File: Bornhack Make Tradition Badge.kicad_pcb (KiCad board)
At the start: 2 copper layers, 100 x 100 mm, 45 parts, among them J1 DEBUG, J2 LE UART, J3 I2C, J4 CONN_02X04, J5 CONN_02X04, J6 CONN_02X04, J7 CONN_01X02, J8 CONN_01X02, P1 USB_OTG, Q1 FDC6420C, SW1 RESET, SW2 POWER, SW3 UP, SW4 DOWN, SW5 RIGHT, SW6 LEFT, U1 EFM32HG322

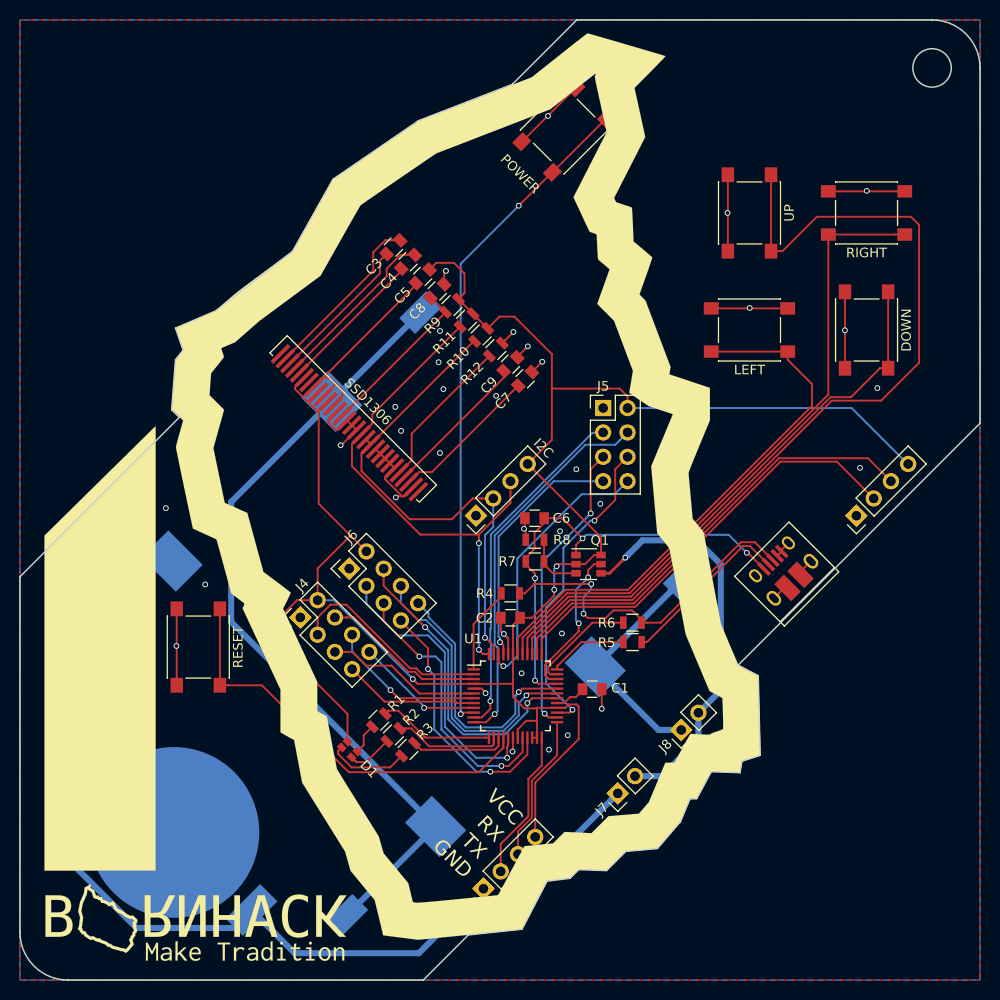
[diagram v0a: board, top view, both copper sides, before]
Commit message: Flipped D+ and D- and removed dual battery option
- D+ and D- has been corrected
- Coin cell holder has been removed, since the badge uses too much power when the screen is on for a coin cell to be a reasonable power source.
- Current measurement pin headers have also been removed.

Signed-off-by: Thomas Flummer <tf@flummer.net>
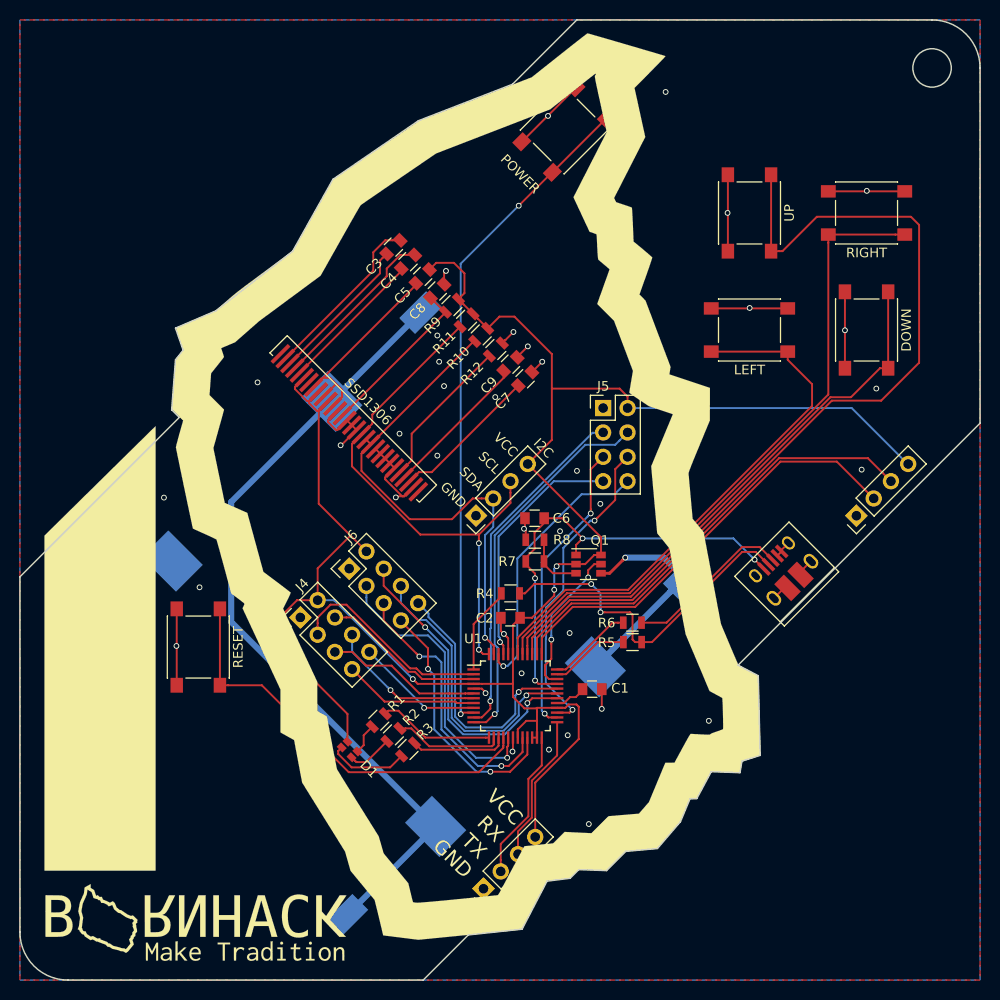
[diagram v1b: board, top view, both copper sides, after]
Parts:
- removed BT1: 3V Button cell, Power:Linx_BAT_HLD_001
- removed J7, J8: CONN_01X02, Pin_Headers:Pin_Header_Straight_1x02_Pitch2.54mm
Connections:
- BT2 pad 1: Net-(BT2-Pad1) -> VBAT
- R4 pad 1: Net-(P1-Pad3) -> Net-(P1-Pad2)
- U1 pad 35: Net-(R6-Pad2) -> Net-(R5-Pad2)
- U1 pad 36: Net-(R5-Pad2) -> Net-(R6-Pad2)
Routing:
- net Net-(BT1-Pad1): track 81.0 -> 0.00 mm
- net Net-(BT2-Pad1): track 24.7 -> 0.00 mm
- net VBAT: track 42.3 -> 23.3 mm
- net Net-(P1-Pad3): track 36.5 -> 17.8 mm, vias 2 -> 0
- net Net-(P1-Pad2): track 18.1 -> 35.9 mm, vias 0 -> 2
- net Net-(R6-Pad2): track 11.3 -> 8.91 mm
- net GND: vias 37 -> 34
- net (no net): vias 0 -> 5
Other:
- board text added: "SCL"
- board text added: "SDA"
- board text removed: "DEVELOPER"
- board text removed: "EDITION"

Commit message: Changed pins for 2 buttons, cleanup and proto pads
- Changed the pins for the LEFT (X) and RIGHT (Y) buttons so that all buttons have their own interrupt
- Changed the name of the buttons to A, B, X and Y so that the names also make sense, when the badge is oriented differently
- Removed silkscreen lines around buttons and non populated pin headers
- Added SMD prototyping area on the back
- Added Open Hardware Logo and CC-BY-SA graphics
- Updated gerber files (production run)

Signed-off-by: Thomas Flummer <tf@flummer.net>
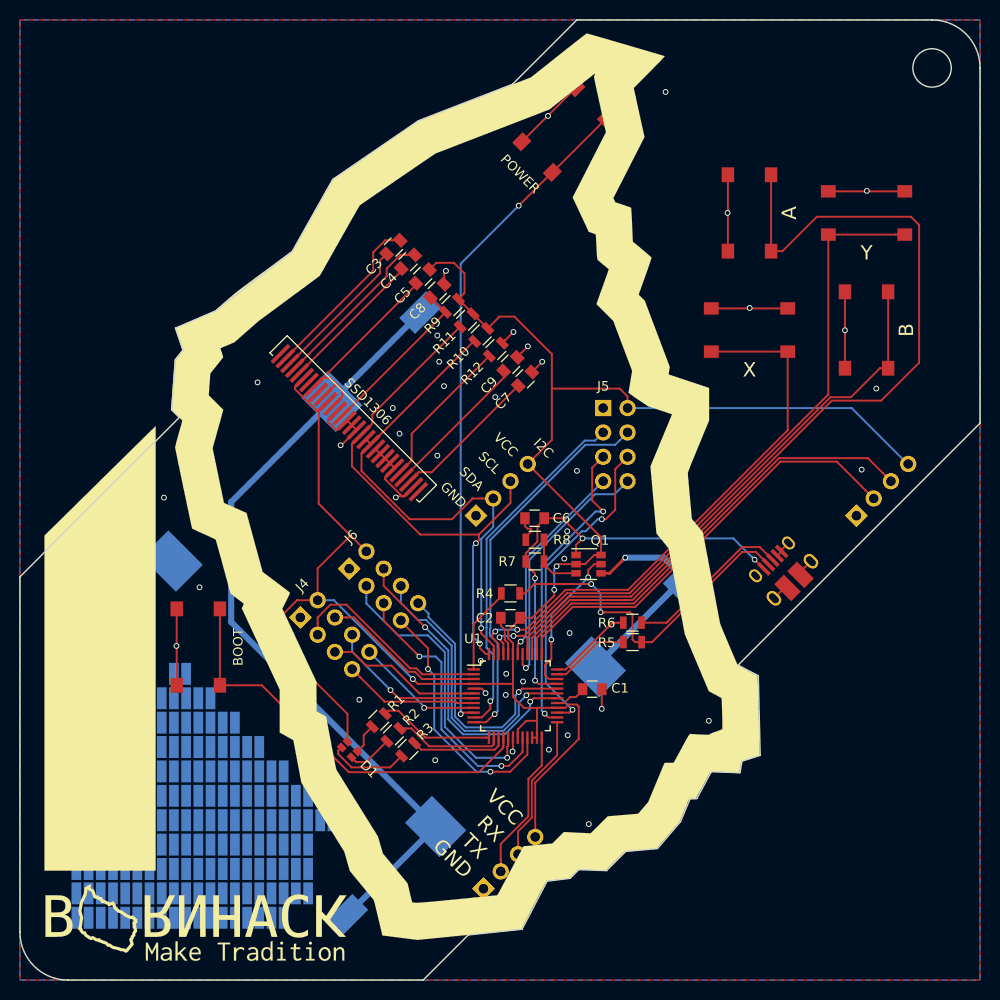
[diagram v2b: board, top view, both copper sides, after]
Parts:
- added G***: LOGO, Aesthetics:oshw_logo_8.3mm, B.Cu at (116.2, 83.3)
- added G***: LOGO, labitat_kicad_footprints:cc-by-sa_badge_8mm, B.Cu at (123.8, 76.2)
- added REF**: SMD Proto pad, ConnectorsTF:SMD_Proto_pad, B.Cu at (82.5, 133.3)
- added REF**: SMD Proto pad, ConnectorsTF:SMD_Proto_pad, B.Cu at (77.5, 128.3)
- added REF**: SMD Proto pad, ConnectorsTF:SMD_Proto_pad, B.Cu at (62.2, 133.3)
- added REF**: SMD Proto pad, ConnectorsTF:SMD_Proto_pad, B.Cu at (61.0, 133.3)
- added REF**: SMD Proto pad, ConnectorsTF:SMD_Proto_pad, B.Cu at (59.7, 133.3)
- added REF**: SMD Proto pad, ConnectorsTF:SMD_Proto_pad, B.Cu at (58.4, 133.3)
- added REF**: SMD Proto pad, ConnectorsTF:SMD_Proto_pad, B.Cu at (57.1, 133.3)
- added REF**: SMD Proto pad, ConnectorsTF:SMD_Proto_pad, B.Cu at (55.9, 133.3)
- added REF**: SMD Proto pad, ConnectorsTF:SMD_Proto_pad, B.Cu at (55.9, 135.9)
- added REF**: SMD Proto pad, ConnectorsTF:SMD_Proto_pad, B.Cu at (57.1, 135.9)
- added REF**: SMD Proto pad, ConnectorsTF:SMD_Proto_pad, B.Cu at (58.4, 135.9)
- added REF**: SMD Proto pad, ConnectorsTF:SMD_Proto_pad, B.Cu at (59.7, 135.9)
- added REF**: SMD Proto pad, ConnectorsTF:SMD_Proto_pad, B.Cu at (74.9, 125.7)
- added REF**: SMD Proto pad, ConnectorsTF:SMD_Proto_pad, B.Cu at (61.0, 135.9)
- added REF**: SMD Proto pad, ConnectorsTF:SMD_Proto_pad, B.Cu at (62.2, 135.9)
- added REF**: SMD Proto pad, ConnectorsTF:SMD_Proto_pad, B.Cu at (63.5, 135.9)
- added REF**: SMD Proto pad, ConnectorsTF:SMD_Proto_pad, B.Cu at (64.8, 135.9)
- added REF**: SMD Proto pad, ConnectorsTF:SMD_Proto_pad, B.Cu at (66.0, 135.9)
- added REF**: SMD Proto pad, ConnectorsTF:SMD_Proto_pad, B.Cu at (67.3, 135.9)
- added REF**: SMD Proto pad, ConnectorsTF:SMD_Proto_pad, B.Cu at (68.6, 135.9)
- added REF**: SMD Proto pad, ConnectorsTF:SMD_Proto_pad, B.Cu at (69.8, 135.9)
- added REF**: SMD Proto pad, ConnectorsTF:SMD_Proto_pad, B.Cu at (71.1, 135.9)
- added REF**: SMD Proto pad, ConnectorsTF:SMD_Proto_pad, B.Cu at (72.4, 135.9)
- added REF**: SMD Proto pad, ConnectorsTF:SMD_Proto_pad, B.Cu at (72.4, 123.2)
- added REF**: SMD Proto pad, ConnectorsTF:SMD_Proto_pad, B.Cu at (73.7, 135.9)
- added REF**: SMD Proto pad, ConnectorsTF:SMD_Proto_pad, B.Cu at (74.9, 135.9)
- added REF**: SMD Proto pad, ConnectorsTF:SMD_Proto_pad, B.Cu at (76.2, 135.9)
- added REF**: SMD Proto pad, ConnectorsTF:SMD_Proto_pad, B.Cu at (77.5, 135.9)
- added REF**: SMD Proto pad, ConnectorsTF:SMD_Proto_pad, B.Cu at (78.7, 135.9)
- added REF**: SMD Proto pad, ConnectorsTF:SMD_Proto_pad, B.Cu at (78.7, 138.4)
- added REF**: SMD Proto pad, ConnectorsTF:SMD_Proto_pad, B.Cu at (77.5, 138.4)
- added REF**: SMD Proto pad, ConnectorsTF:SMD_Proto_pad, B.Cu at (76.2, 138.4)
- added REF**: SMD Proto pad, ConnectorsTF:SMD_Proto_pad, B.Cu at (74.9, 138.4)
- added REF**: SMD Proto pad, ConnectorsTF:SMD_Proto_pad, B.Cu at (73.7, 138.4)
- added REF**: SMD Proto pad, ConnectorsTF:SMD_Proto_pad, B.Cu at (69.8, 120.7)
- added REF**: SMD Proto pad, ConnectorsTF:SMD_Proto_pad, B.Cu at (71.1, 138.4)
- added REF**: SMD Proto pad, ConnectorsTF:SMD_Proto_pad, B.Cu at (72.4, 138.4)
- added REF**: SMD Proto pad, ConnectorsTF:SMD_Proto_pad, B.Cu at (69.8, 138.4)
- added REF**: SMD Proto pad, ConnectorsTF:SMD_Proto_pad, B.Cu at (68.6, 138.4)
- added REF**: SMD Proto pad, ConnectorsTF:SMD_Proto_pad, B.Cu at (67.3, 138.4)
- added REF**: SMD Proto pad, ConnectorsTF:SMD_Proto_pad, B.Cu at (66.0, 138.4)
- added REF**: SMD Proto pad, ConnectorsTF:SMD_Proto_pad, B.Cu at (64.8, 138.4)
- added REF**: SMD Proto pad, ConnectorsTF:SMD_Proto_pad, B.Cu at (63.5, 138.4)
- added REF**: SMD Proto pad, ConnectorsTF:SMD_Proto_pad, B.Cu at (62.2, 138.4)
- added REF**: SMD Proto pad, ConnectorsTF:SMD_Proto_pad, B.Cu at (61.0, 138.4)
- added REF**: SMD Proto pad, ConnectorsTF:SMD_Proto_pad, B.Cu at (68.6, 120.7)
- added REF**: SMD Proto pad, ConnectorsTF:SMD_Proto_pad, B.Cu at (59.7, 138.4)
- added REF**: SMD Proto pad, ConnectorsTF:SMD_Proto_pad, B.Cu at (58.4, 138.4)
- added REF**: SMD Proto pad, ConnectorsTF:SMD_Proto_pad, B.Cu at (57.1, 138.4)
- added REF**: SMD Proto pad, ConnectorsTF:SMD_Proto_pad, B.Cu at (55.9, 138.4)
- added REF**: SMD Proto pad, ConnectorsTF:SMD_Proto_pad, B.Cu at (63.5, 141.0)
- added REF**: SMD Proto pad, ConnectorsTF:SMD_Proto_pad, B.Cu at (64.8, 141.0)
- added REF**: SMD Proto pad, ConnectorsTF:SMD_Proto_pad, B.Cu at (66.0, 141.0)
- added REF**: SMD Proto pad, ConnectorsTF:SMD_Proto_pad, B.Cu at (67.3, 141.0)
- added REF**: SMD Proto pad, ConnectorsTF:SMD_Proto_pad, B.Cu at (68.6, 141.0)
- added REF**: SMD Proto pad, ConnectorsTF:SMD_Proto_pad, B.Cu at (69.8, 141.0)
- added REF**: SMD Proto pad, ConnectorsTF:SMD_Proto_pad, B.Cu at (67.3, 120.7)
- added REF**: SMD Proto pad, ConnectorsTF:SMD_Proto_pad, B.Cu at (71.1, 141.0)
- added REF**: SMD Proto pad, ConnectorsTF:SMD_Proto_pad, B.Cu at (72.4, 141.0)
- added REF**: SMD Proto pad, ConnectorsTF:SMD_Proto_pad, B.Cu at (73.7, 141.0)
- added REF**: SMD Proto pad, ConnectorsTF:SMD_Proto_pad, B.Cu at (74.9, 141.0)
- added REF**: SMD Proto pad, ConnectorsTF:SMD_Proto_pad, B.Cu at (76.2, 141.0)
- added REF**: SMD Proto pad, ConnectorsTF:SMD_Proto_pad, B.Cu at (77.5, 141.0)
- added REF**: SMD Proto pad, ConnectorsTF:SMD_Proto_pad, B.Cu at (78.7, 141.0)
- added REF**: SMD Proto pad, ConnectorsTF:SMD_Proto_pad, B.Cu at (77.5, 143.5)
- added REF**: SMD Proto pad, ConnectorsTF:SMD_Proto_pad, B.Cu at (76.2, 143.5)
- added REF**: SMD Proto pad, ConnectorsTF:SMD_Proto_pad, B.Cu at (74.9, 143.5)
- added REF**: SMD Proto pad, ConnectorsTF:SMD_Proto_pad, B.Cu at (66.0, 120.7)
- added REF**: SMD Proto pad, ConnectorsTF:SMD_Proto_pad, B.Cu at (73.7, 143.5)
- added REF**: SMD Proto pad, ConnectorsTF:SMD_Proto_pad, B.Cu at (72.4, 143.5)
- added REF**: SMD Proto pad, ConnectorsTF:SMD_Proto_pad, B.Cu at (71.1, 143.5)
- added REF**: SMD Proto pad, ConnectorsTF:SMD_Proto_pad, B.Cu at (69.8, 143.5)
- added REF**: SMD Proto pad, ConnectorsTF:SMD_Proto_pad, B.Cu at (68.6, 143.5)
- added REF**: SMD Proto pad, ConnectorsTF:SMD_Proto_pad, B.Cu at (67.3, 143.5)
- added REF**: SMD Proto pad, ConnectorsTF:SMD_Proto_pad, B.Cu at (66.0, 143.5)
- added REF**: SMD Proto pad, ConnectorsTF:SMD_Proto_pad, B.Cu at (64.8, 143.5)
- added REF**: SMD Proto pad, ConnectorsTF:SMD_Proto_pad, B.Cu at (63.5, 143.5)
- added REF**: SMD Proto pad, ConnectorsTF:SMD_Proto_pad, B.Cu at (55.9, 141.0)
- added REF**: SMD Proto pad, ConnectorsTF:SMD_Proto_pad, B.Cu at (64.8, 120.7)
- added REF**: SMD Proto pad, ConnectorsTF:SMD_Proto_pad, B.Cu at (57.1, 141.0)
- added REF**: SMD Proto pad, ConnectorsTF:SMD_Proto_pad, B.Cu at (58.4, 141.0)
- added REF**: SMD Proto pad, ConnectorsTF:SMD_Proto_pad, B.Cu at (59.7, 141.0)
- added REF**: SMD Proto pad, ConnectorsTF:SMD_Proto_pad, B.Cu at (61.0, 141.0)
- added REF**: SMD Proto pad, ConnectorsTF:SMD_Proto_pad, B.Cu at (62.2, 141.0)
- added REF**: SMD Proto pad, ConnectorsTF:SMD_Proto_pad, B.Cu at (62.2, 143.5)
- added REF**: SMD Proto pad, ConnectorsTF:SMD_Proto_pad, B.Cu at (61.0, 143.5)
- added REF**: SMD Proto pad, ConnectorsTF:SMD_Proto_pad, B.Cu at (59.7, 143.5)
- added REF**: SMD Proto pad, ConnectorsTF:SMD_Proto_pad, B.Cu at (58.4, 143.5)
- added REF**: SMD Proto pad, ConnectorsTF:SMD_Proto_pad, B.Cu at (57.1, 143.5)
- added REF**: SMD Proto pad, ConnectorsTF:SMD_Proto_pad, B.Cu at (63.5, 120.7)
- added REF**: SMD Proto pad, ConnectorsTF:SMD_Proto_pad, B.Cu at (55.9, 143.5)
- added REF**: SMD Proto pad, ConnectorsTF:SMD_Proto_pad, B.Cu at (62.2, 120.7)
- added REF**: SMD Proto pad, ConnectorsTF:SMD_Proto_pad, B.Cu at (81.3, 133.3)
- added REF**: SMD Proto pad, ConnectorsTF:SMD_Proto_pad, B.Cu at (61.0, 120.7)
- added REF**: SMD Proto pad, ConnectorsTF:SMD_Proto_pad, B.Cu at (59.7, 120.7)
- added REF**: SMD Proto pad, ConnectorsTF:SMD_Proto_pad, B.Cu at (58.4, 120.7)
- added REF**: SMD Proto pad, ConnectorsTF:SMD_Proto_pad, B.Cu at (71.1, 123.2)
- added REF**: SMD Proto pad, ConnectorsTF:SMD_Proto_pad, B.Cu at (69.8, 123.2)
- added REF**: SMD Proto pad, ConnectorsTF:SMD_Proto_pad, B.Cu at (68.6, 123.2)
- added REF**: SMD Proto pad, ConnectorsTF:SMD_Proto_pad, B.Cu at (67.3, 123.2)
- added REF**: SMD Proto pad, ConnectorsTF:SMD_Proto_pad, B.Cu at (66.0, 123.2)
- added REF**: SMD Proto pad, ConnectorsTF:SMD_Proto_pad, B.Cu at (64.8, 123.2)
- added REF**: SMD Proto pad, ConnectorsTF:SMD_Proto_pad, B.Cu at (63.5, 123.2)
- added REF**: SMD Proto pad, ConnectorsTF:SMD_Proto_pad, B.Cu at (66.0, 118.1)
- added REF**: SMD Proto pad, ConnectorsTF:SMD_Proto_pad, B.Cu at (62.2, 123.2)
- added REF**: SMD Proto pad, ConnectorsTF:SMD_Proto_pad, B.Cu at (61.0, 123.2)
- added REF**: SMD Proto pad, ConnectorsTF:SMD_Proto_pad, B.Cu at (59.7, 123.2)
- added REF**: SMD Proto pad, ConnectorsTF:SMD_Proto_pad, B.Cu at (58.4, 123.2)
- added REF**: SMD Proto pad, ConnectorsTF:SMD_Proto_pad, B.Cu at (57.1, 123.2)
- added REF**: SMD Proto pad, ConnectorsTF:SMD_Proto_pad, B.Cu at (55.9, 123.2)
- added REF**: SMD Proto pad, ConnectorsTF:SMD_Proto_pad, B.Cu at (55.9, 125.7)
- added REF**: SMD Proto pad, ConnectorsTF:SMD_Proto_pad, B.Cu at (57.1, 125.7)
- added REF**: SMD Proto pad, ConnectorsTF:SMD_Proto_pad, B.Cu at (58.4, 125.7)
- added REF**: SMD Proto pad, ConnectorsTF:SMD_Proto_pad, B.Cu at (59.7, 125.7)
- added REF**: SMD Proto pad, ConnectorsTF:SMD_Proto_pad, B.Cu at (67.3, 118.1)
- added REF**: SMD Proto pad, ConnectorsTF:SMD_Proto_pad, B.Cu at (61.0, 125.7)
- added REF**: SMD Proto pad, ConnectorsTF:SMD_Proto_pad, B.Cu at (62.2, 125.7)
- added REF**: SMD Proto pad, ConnectorsTF:SMD_Proto_pad, B.Cu at (63.5, 125.7)
- added REF**: SMD Proto pad, ConnectorsTF:SMD_Proto_pad, B.Cu at (64.8, 125.7)
- added REF**: SMD Proto pad, ConnectorsTF:SMD_Proto_pad, B.Cu at (66.0, 125.7)
- added REF**: SMD Proto pad, ConnectorsTF:SMD_Proto_pad, B.Cu at (68.6, 125.7)
- added REF**: SMD Proto pad, ConnectorsTF:SMD_Proto_pad, B.Cu at (67.3, 125.7)
- added REF**: SMD Proto pad, ConnectorsTF:SMD_Proto_pad, B.Cu at (69.8, 125.7)
- added REF**: SMD Proto pad, ConnectorsTF:SMD_Proto_pad, B.Cu at (71.1, 125.7)
- added REF**: SMD Proto pad, ConnectorsTF:SMD_Proto_pad, B.Cu at (72.4, 125.7)
- added REF**: SMD Proto pad, ConnectorsTF:SMD_Proto_pad, B.Cu at (80.0, 141.0)
- added REF**: SMD Proto pad, ConnectorsTF:SMD_Proto_pad, B.Cu at (73.7, 125.7)
- added REF**: SMD Proto pad, ConnectorsTF:SMD_Proto_pad, B.Cu at (76.2, 128.3)
- added REF**: SMD Proto pad, ConnectorsTF:SMD_Proto_pad, B.Cu at (74.9, 128.3)
- added REF**: SMD Proto pad, ConnectorsTF:SMD_Proto_pad, B.Cu at (73.7, 128.3)
- added REF**: SMD Proto pad, ConnectorsTF:SMD_Proto_pad, B.Cu at (72.4, 128.3)
- added REF**: SMD Proto pad, ConnectorsTF:SMD_Proto_pad, B.Cu at (71.1, 128.3)
- added REF**: SMD Proto pad, ConnectorsTF:SMD_Proto_pad, B.Cu at (69.8, 128.3)
- added REF**: SMD Proto pad, ConnectorsTF:SMD_Proto_pad, B.Cu at (68.6, 128.3)
- added REF**: SMD Proto pad, ConnectorsTF:SMD_Proto_pad, B.Cu at (67.3, 128.3)
- added REF**: SMD Proto pad, ConnectorsTF:SMD_Proto_pad, B.Cu at (66.0, 128.3)
- added REF**: SMD Proto pad, ConnectorsTF:SMD_Proto_pad, B.Cu at (80.0, 138.4)
- added REF**: SMD Proto pad, ConnectorsTF:SMD_Proto_pad, B.Cu at (64.8, 128.3)
- added REF**: SMD Proto pad, ConnectorsTF:SMD_Proto_pad, B.Cu at (63.5, 128.3)
- added REF**: SMD Proto pad, ConnectorsTF:SMD_Proto_pad, B.Cu at (62.2, 128.3)
- added REF**: SMD Proto pad, ConnectorsTF:SMD_Proto_pad, B.Cu at (61.0, 128.3)
- added REF**: SMD Proto pad, ConnectorsTF:SMD_Proto_pad, B.Cu at (59.7, 128.3)
- added REF**: SMD Proto pad, ConnectorsTF:SMD_Proto_pad, B.Cu at (58.4, 128.3)
- added REF**: SMD Proto pad, ConnectorsTF:SMD_Proto_pad, B.Cu at (57.1, 128.3)
- added REF**: SMD Proto pad, ConnectorsTF:SMD_Proto_pad, B.Cu at (55.9, 128.3)
- added REF**: SMD Proto pad, ConnectorsTF:SMD_Proto_pad, B.Cu at (55.9, 130.8)
- added REF**: SMD Proto pad, ConnectorsTF:SMD_Proto_pad, B.Cu at (57.1, 130.8)
- added REF**: SMD Proto pad, ConnectorsTF:SMD_Proto_pad, B.Cu at (80.0, 135.9)
- added REF**: SMD Proto pad, ConnectorsTF:SMD_Proto_pad, B.Cu at (59.7, 130.8)
- added REF**: SMD Proto pad, ConnectorsTF:SMD_Proto_pad, B.Cu at (58.4, 130.8)
- added REF**: SMD Proto pad, ConnectorsTF:SMD_Proto_pad, B.Cu at (61.0, 130.8)
- added REF**: SMD Proto pad, ConnectorsTF:SMD_Proto_pad, B.Cu at (62.2, 130.8)
- added REF**: SMD Proto pad, ConnectorsTF:SMD_Proto_pad, B.Cu at (63.5, 130.8)
- added REF**: SMD Proto pad, ConnectorsTF:SMD_Proto_pad, B.Cu at (64.8, 130.8)
- added REF**: SMD Proto pad, ConnectorsTF:SMD_Proto_pad, B.Cu at (66.0, 130.8)
- added REF**: SMD Proto pad, ConnectorsTF:SMD_Proto_pad, B.Cu at (67.3, 130.8)
- added REF**: SMD Proto pad, ConnectorsTF:SMD_Proto_pad, B.Cu at (68.6, 130.8)
- added REF**: SMD Proto pad, ConnectorsTF:SMD_Proto_pad, B.Cu at (69.8, 130.8)
- added REF**: SMD Proto pad, ConnectorsTF:SMD_Proto_pad, B.Cu at (80.0, 133.3)
- added REF**: SMD Proto pad, ConnectorsTF:SMD_Proto_pad, B.Cu at (71.1, 130.8)
- added REF**: SMD Proto pad, ConnectorsTF:SMD_Proto_pad, B.Cu at (72.4, 130.8)
- added REF**: SMD Proto pad, ConnectorsTF:SMD_Proto_pad, B.Cu at (73.7, 130.8)
- added REF**: SMD Proto pad, ConnectorsTF:SMD_Proto_pad, B.Cu at (74.9, 130.8)
- added REF**: SMD Proto pad, ConnectorsTF:SMD_Proto_pad, B.Cu at (76.2, 130.8)
- added REF**: SMD Proto pad, ConnectorsTF:SMD_Proto_pad, B.Cu at (77.5, 130.8)
- added REF**: SMD Proto pad, ConnectorsTF:SMD_Proto_pad, B.Cu at (78.7, 130.8)
- added REF**: SMD Proto pad, ConnectorsTF:SMD_Proto_pad, B.Cu at (78.7, 133.3)
- added REF**: SMD Proto pad, ConnectorsTF:SMD_Proto_pad, B.Cu at (77.5, 133.3)
- added REF**: SMD Proto pad, ConnectorsTF:SMD_Proto_pad, B.Cu at (76.2, 133.3)
- added REF**: SMD Proto pad, ConnectorsTF:SMD_Proto_pad, B.Cu at (80.0, 130.8)
- added REF**: SMD Proto pad, ConnectorsTF:SMD_Proto_pad, B.Cu at (74.9, 133.3)
- added REF**: SMD Proto pad, ConnectorsTF:SMD_Proto_pad, B.Cu at (73.7, 133.3)
- added REF**: SMD Proto pad, ConnectorsTF:SMD_Proto_pad, B.Cu at (72.4, 133.3)
- added REF**: SMD Proto pad, ConnectorsTF:SMD_Proto_pad, B.Cu at (71.1, 133.3)
- added REF**: SMD Proto pad, ConnectorsTF:SMD_Proto_pad, B.Cu at (69.8, 133.3)
- added REF**: SMD Proto pad, ConnectorsTF:SMD_Proto_pad, B.Cu at (68.6, 133.3)
- added REF**: SMD Proto pad, ConnectorsTF:SMD_Proto_pad, B.Cu at (67.3, 133.3)
- added REF**: SMD Proto pad, ConnectorsTF:SMD_Proto_pad, B.Cu at (66.0, 133.3)
- added REF**: SMD Proto pad, ConnectorsTF:SMD_Proto_pad, B.Cu at (64.8, 133.3)
- added REF**: SMD Proto pad, ConnectorsTF:SMD_Proto_pad, B.Cu at (63.5, 133.3)
- R2: value 1K -> 1.2K
- R3: value 1K -> 820
- SW1: value RESET -> BOOT
- SW3: value UP -> A
- SW4: value DOWN -> B
- SW5: value RIGHT -> Y
- SW6: value LEFT -> X
- moved G*** 0.08 mm to (101.9, 99.0)
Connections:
- net DOWN renamed BUTTON_B
- net UP renamed BUTTON_A
- J5 pad 7: PE10 -> PF5
- J5 pad 8: PE11 -> PF4
- SW5 pad 2: RIGHT -> BUTTON_Y
- SW6 pad 2: LEFT -> BUTTON_X
- U1 pad 41: RIGHT -> PF4
- U1 pad 42: LEFT -> PF5
- U1 pad 45: PE10 -> BUTTON_Y
- U1 pad 46: PE11 -> BUTTON_X
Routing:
- net BUTTON_Y: track 0.00 -> 71.3 mm, vias 0 -> 2
- net RIGHT: track 68.7 -> 0.00 mm
- net BUTTON_X: track 0.00 -> 58.0 mm, vias 0 -> 2
- net LEFT: track 57.0 -> 0.00 mm
- net PE11: track 28.4 -> 0.00 mm, vias 1 -> 0
- net PF4: track 0.00 -> 26.6 mm, vias 0 -> 1
- net PE10: track 25.7 -> 0.00 mm, vias 1 -> 0
- net PF5: track 0.00 -> 21.7 mm, vias 0 -> 1
- net PD6: track 31.0 -> 32.4 mm
- net GND: track 88.6 -> 89.2 mm, vias 34 -> 40
- net PB7: track 36.4 -> 37.0 mm
- net (no net): vias 5 -> 2
